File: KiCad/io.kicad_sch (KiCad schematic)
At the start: 72 parts, among them Q401 BC857W, Q402 BC857W, Q403 BC857W, Q404 BC857W, Q405 BC857W, SW401 SW_DIP_x04, SW402 SW_DIP_x04, SW403 SW_Omron_B3FS, SW404 SW_Omron_B3FS, SW405 SW_Omron_B3FS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

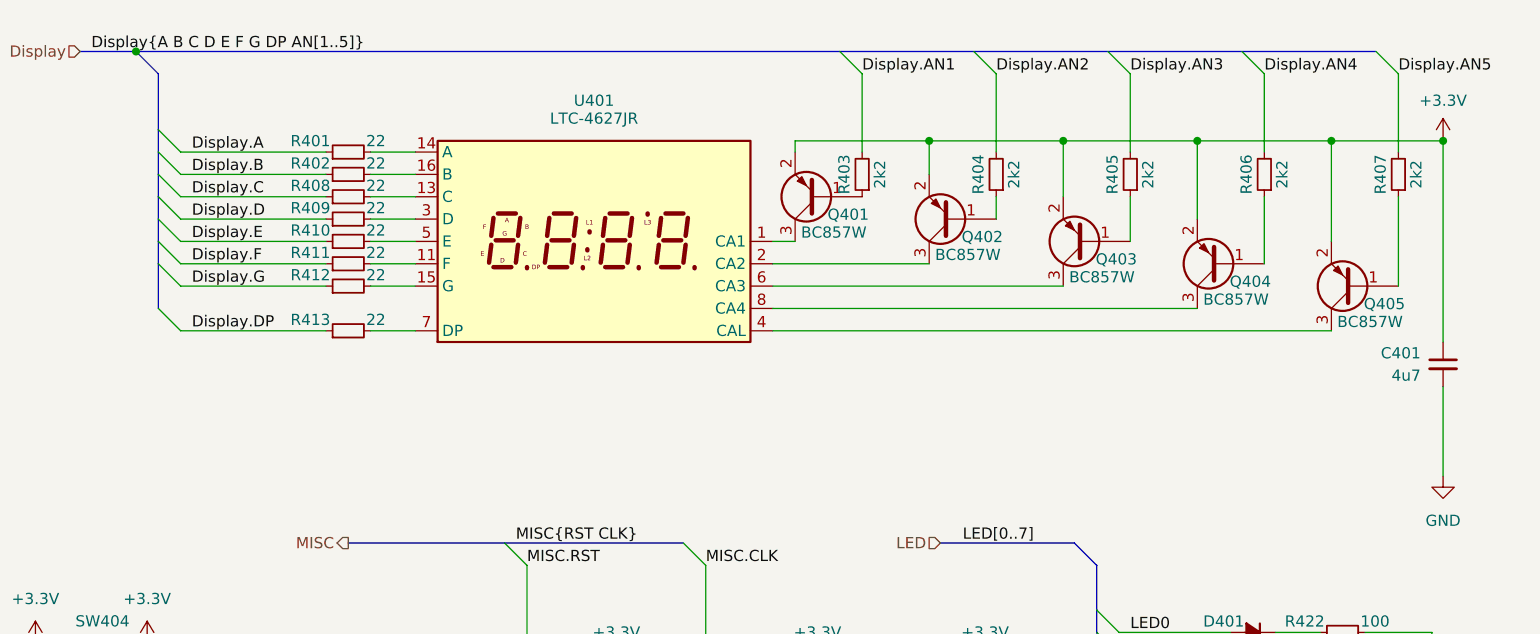
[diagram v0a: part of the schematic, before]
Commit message: kleine Anpassungen im Silkscreen
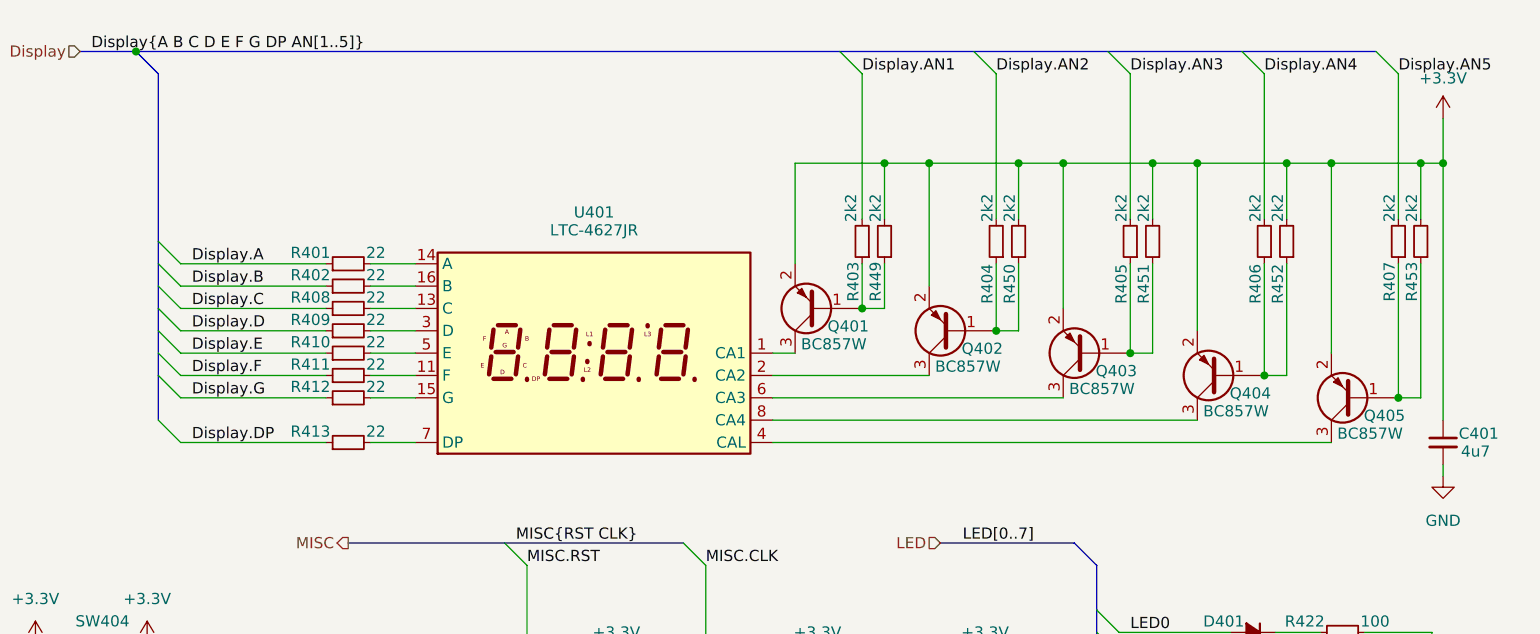
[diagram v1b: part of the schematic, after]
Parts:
- added R449, R450, R451, R452, R453: 2k2, Resistor_SMD:R_0402_1005Metric, symbol Device:R_Small
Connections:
- net +3.3V: now also R449.2, R450.2, R451.2, R452.2, R453.2
- net at Q403.1 (B), R405.1: now also R451.1
- net at Q404.1 (B), R406.1: now also R452.1
- net at Q402.1 (B), R404.1: now also R450.1
- net at Q405.1 (B), R407.1: now also R453.1
- net at Q401.1 (B), R403.1: now also R449.1
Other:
- moved on the sheet: C401, Q401, Q402, Q403, Q404, Q405, R401, R402, R403, R404, R405, R406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
